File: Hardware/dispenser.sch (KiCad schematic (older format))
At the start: 60 parts, among them J1 Vin, J2 encoder+btn, J3 YuMi_interface, J4 Motor, U1 SN74LVC1G14, U2 LM2675, U3 PC817, U4 ATMEGA328P-AU-Arduino, U5 PC817, U6 A4973, U7 PC817, U8 SN74LVC1G14, U9 SN74LVC1G14, Y1 8MHZ

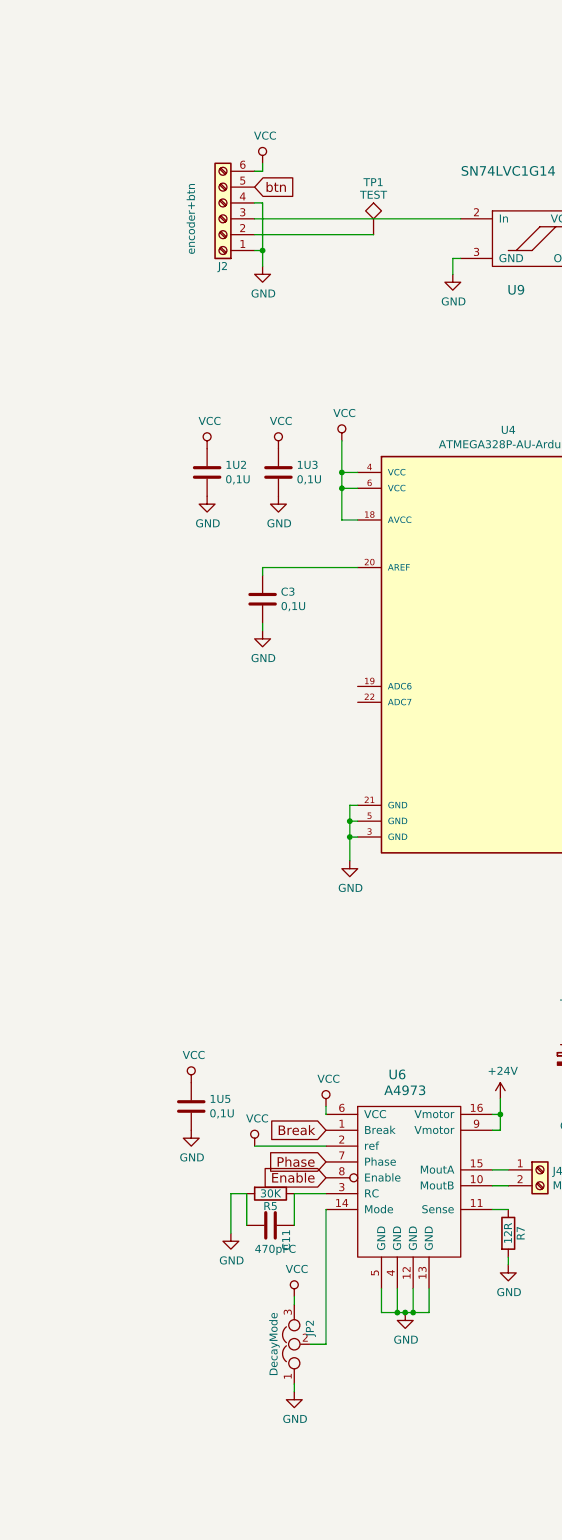
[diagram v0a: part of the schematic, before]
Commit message: added limitswitches
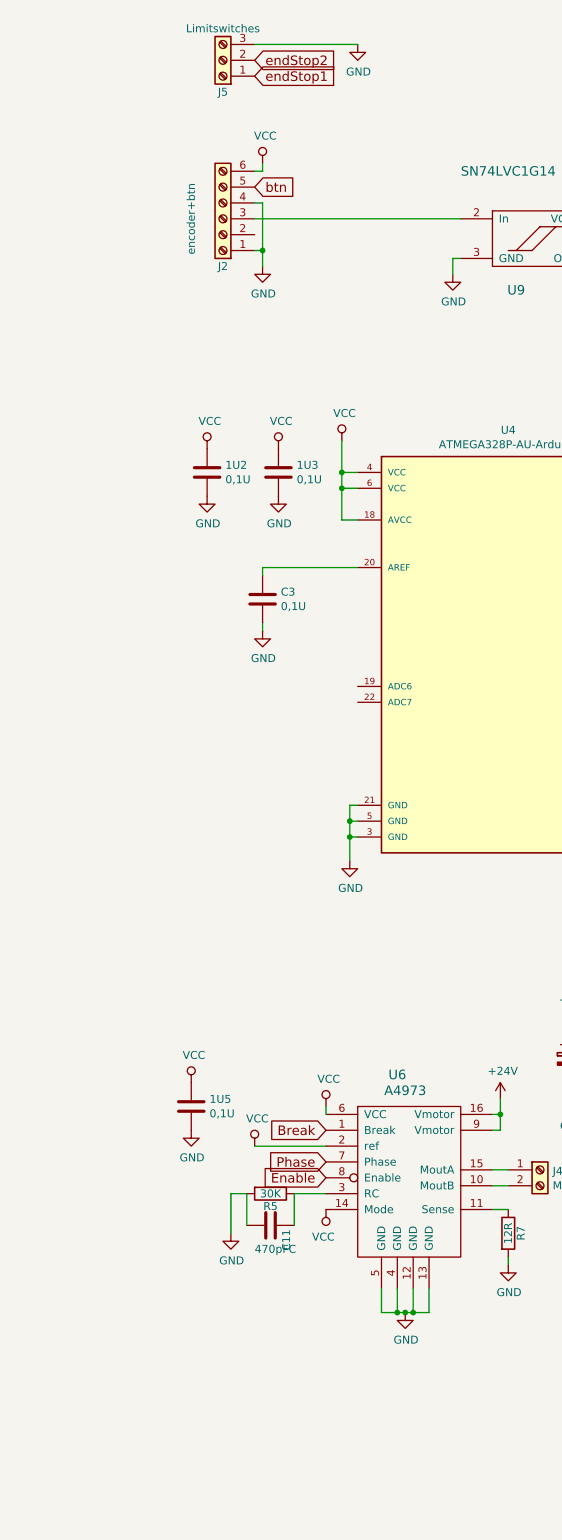
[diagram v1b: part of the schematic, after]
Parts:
- removed JP2: DecayMode, jumper:SOLDER-JUMPER_2-WAY, symbol Jumper_NC_Dual
- removed TP1: TEST, Socket_Strips:Socket_Strip_Angled_1x01_Pitch2.54mm, symbol TEST
- added J5: Limitswitches, Pin_Headers:Pin_Header_Straight_1x03_Pitch2.54mm, symbol Screw_Terminal_01x03
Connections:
- net GND: now also J5.3 (Pin_3)
- net VCC: now also U6.14 (Mode)
- new net endStop1: J5.1 (Pin_1)
- new net endStop2: J5.2 (Pin_2)
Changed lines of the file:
@@
 LIBS:L298N
 LIBS:WS2812B
+LIBS:a4973
 LIBS:dispenser-cache
 EELAYER 25 0
@@
 	11600 1800 11600 2200
 Wire Wire Line
-	11550 2000 12300 2000
-Wire Wire Line
 	1700 1250 1700 1450
 Wire Wire Line
@@
 	14050 7000 14050 7050
 $Comp
-L Jumper_NC_Dual JP2
-U 1 1 5A0A3D14
-P 11800 9000
-F 0 "JP2" H 11850 8900 50  0000 L CNN
-F 1 "DecayMode" H 11800 9100 50  0000 C BNN
-F 2 "jumper:SOLDER-JUMPER_2-WAY" H 11800 9000 50  0001 C CNN
-F 3 "" H 11800 9000 50  0001 C CNN
-	1    11800 9000
-	0    -1   -1   0
-$EndComp
-$Comp
-L GND #PWR044
-U 1 1 5A0A3E41
-P 11800 9300
-F 0 "#PWR044" H 11800 9050 50  0001 C CNN
-F 1 "GND" H 11805 9127 50  0000 C CNN
-F 2 "" H 11800 9300 50  0001 C CNN
-F 3 "" H 11800 9300 50  0001 C CNN
-	1    11800 9300
-	1    0    0    -1
-$EndComp
-Wire Wire Line
-	11800 9250 11800 9300
-$Comp
 L VCC #PWR045
 U 1 1 5A0A4017
-P 11800 8700
-F 0 "#PWR045" H 11800 8550 50  0001 C CNN
-F 1 "VCC" H 11817 8873 50  0000 C CNN
-F 2 "" H 11800 8700 50  0001 C CNN
-F 3 "" H 11800 8700 50  0001 C CNN
-	1    11800 8700
-	1    0    0    -1
-$EndComp
-Wire Wire Line
-	11800 8750 11800 8700
-Wire Wire Line
-	11900 9000 12000 9000
-Wire Wire Line
-	12000 9000 12000 8150
+P 12000 8150
+F 0 "#PWR045" H 12000 8000 50  0001 C CNN
+F 1 "VCC" H 12017 8323 50  0000 C CNN
+F 2 "" H 12000 8150 50  0001 C CNN
+F 3 "" H 12000 8150 50  0001 C CNN
+	1    12000 8150
+	-1   0    0    1
+$EndComp
 $Comp
 L R R7
@@
 	12800 2150 12800 2250
 $Comp
-L TEST TP1
-U 1 1 5A0B3992
-P 12300 2000
-F 0 "TP1" H 12300 2300 50  0000 C BNN
-F 1 "TEST" H 12300 2250 50  0000 C CNN
-F 2 "Socket_Strips:Socket_Strip_Angled_1x01_Pitch2.54mm" H 12300 2000 50  0001 C CNN
-F 3 "" H 12300 2000 50  0001 C CNN
-	1    12300 2000
-	1    0    0    -1
-$EndComp
-$Comp
 L LM2675 U2
 U 1 1 5A169D00
@@
 Wire Notes Line
 	5650 10950 3200 10950
+$Comp
+L Screw_Terminal_01x03 J5
+U 1 1 5A1FD8A3
+P 11350 900
+F 0 "J5" H 11350 1100 50  0000 C CNN
+F 1 "Limitswitches" H 11350 700 50  0000 C CNN
+F 2 "Pin_Headers:Pin_Header_Straight_1x03_Pitch2.54mm" H 11350 900 50  0001 C CNN
+F 3 "" H 11350 900 50  0001 C CNN
+	1    11350 900
+	-1   0    0    1
+$EndComp
+Text GLabel 11550 1000 2    60   Input ~ 0
+endStop1
+Text GLabel 11550 900  2    60   Input ~ 0
+endStop2
+$Comp
+L GND #PWR062
+U 1 1 5A1FDD4B
+P 12200 800
+F 0 "#PWR062" H 12200 550 50  0001 C CNN
+F 1 "GND" H 12205 627 50  0000 C CNN
+F 2 "" H 12200 800 50  0001 C CNN
+F 3 "" H 12200 800 50  0001 C CNN
+	1    12200 800
+	1    0    0    -1
+$EndComp
+Wire Wire Line
+	12200 800  11550 800
 $EndSCHEMATC

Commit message: sync old atmega files
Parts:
- removed C11: 470pFC, Capacitors_SMD:C_0805_HandSoldering, symbol C
- removed C12: 47uf, Capacitors_Tantalum_SMD:CP_Tantalum_Case-D_EIA-7343-31_Hand, symbol CP
- removed C13: 330Uf, Capacitors_SMD:CP_Elec_10x10, symbol CP
- removed C7: 4.7uF tant, Capacitors_Tantalum_SMD:CP_Tantalum_Case-C_EIA-6032-28_Hand, symbol CP
- removed C8: 10nf, Capacitors_SMD:C_0805_HandSoldering, symbol C_Small
- removed D5: D_Schottky, Diodes_SMD:D_SMC_Handsoldering, symbol D_Schottky
- removed J2: encoder+btn, Pin_Headers:Pin_Header_Straight_1x06_Pitch2.54mm, symbol Screw_Terminal_01x06
- removed J5: Limitswitches, Pin_Headers:Pin_Header_Straight_1x03_Pitch2.54mm, symbol Screw_Terminal_01x03
- removed L1: 47uH, Inductors_SMD:L_7.3x7.3_H4.5, symbol L
- removed R10: 3K, Resistors_SMD:R_0805_HandSoldering, symbol R
- removed U1, U8, U9: SN74LVC1G14, TO_SOT_Packages_SMD:SOT-23-5_HandSoldering, symbol SN74LVC1G14
- removed U2: LM2675, Housings_SOIC:SOIC-8_3.9x4.9mm_Pitch1.27mm, symbol LM2675
- removed U6: A4973, Housings_SOIC:SOIC-16W_7.5x10.3mm_Pitch1.27mm, symbol A4973
- added C7, C8: 47nF, Capacitors_SMD:C_0805_HandSoldering, symbol C
- added D6, D7, D8, D9: D, Diodes_SMD:D_SMA-SMB_Universal_Handsoldering, symbol D
- added IC1: L298N, Libs:Multiwatt15_V, symbol L298N
- added ISP1: ISP-header, Pin_Headers:Pin_Header_Straight_2x03_Pitch2.54mm, symbol ISP-header
- added J2: encoder_in, Socket_Strips:Socket_Strip_Straight_1x04_Pitch2.54mm, symbol Screw_Terminal_01x04
- added J5: OELD, Pin_Headers:Pin_Header_Straight_1x04_Pitch2.54mm, symbol Conn_01x04
- added R13, R14: 100K, Resistors_SMD:R_0805_HandSoldering, symbol R
- added R17, R18: 4k7, Resistors_SMD:R_0805_HandSoldering, symbol R
- added U1: 74HC14, Housings_DIP:DIP-14_W7.62mm_LongPads, symbol 74HC14
- added U2: AMS117-5.0, TO_SOT_Packages_SMD:SOT-223, symbol AMS117-5.0
- added U6: LM321, TO_SOT_Packages_SMD:SOT-23-5, symbol LM321
- 1U1: value 0.1uf -> 1U
- C1: value 4.7uF tant -> 22uf; footprint Capacitors_Tantalum_SMD:CP_Tantalum_Case-C_EIA-6032-28_Hand -> Capacitors_Tantalum_SMD:CP_Tantalum_Case-D_EIA-7343-31_Hand
- C5: value 47uf -> 22uf
- D2, D4: footprint LEDs:LED_0805_HandSoldering -> LEDs:LED_D3.0mm
- JP1: footprint Pin_Headers:Pin_Header_Straight_2x01_Pitch2.54mm -> jumper:SOLDER-JUMPER_1-WAY
- R5: value 30K -> 330K
- R7: value 12R -> 6k8
- R8: value 1K -> 1R; footprint Resistors_SMD:R_0805_HandSoldering -> Resistors_THT:R_Axial_DIN0516_L15.5mm_D5.0mm_P20.32mm_Horizontal
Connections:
- net +24V: now also D6.1 (K), D7.1 (K), IC1.4 (VS), U2.3 (Vin); no longer C1.1
- net CMD: now also U1.8
- net GND: now also C7.2, C8.2, D8.2 (A), D9.2 (A), IC1.10 (INPUT3), IC1.11 (ENABLE_B), IC1.12 (INPUT4), IC1.15 (SEN_B), IC1.8 (GND), ISP1.6 (GND), J2.1 (Pin_1), J5.4 (Pin_4), U1.11, U1.13, U1.7 (GND), U1.7 (GND), U1.7 (GND), U1.7 (GND), U1.7 (GND), U1.7 (GND), U2.1 (GND), U6.2 (V-); no longer D3.1 (VSS), R5.2
- net LED: no longer D3.2 (DIN)
- net MISO: now also ISP1.1 (MISO)
- net MOSI: now also ISP1.4 (MOSI)
- net SCK: now also ISP1.3 (SCK)
- net Step: now also U1.6
- net VCC: now also C1.1, IC1.9 (VCC), ISP1.2 (VCC), J2.4 (Pin_4), J5.1 (Pin_1), R13.1, R14.1, R17.1, R18.1, U1.14 (VCC), U1.14 (VCC), U1.14 (VCC), U1.14 (VCC), U1.14 (VCC), U1.14 (VCC), U2.2 (Vout), U6.5 (V+); no longer D3.3 (VDD)
- net encA: now also U1.2
- net reset_in: now also ISP1.5 (RST)
- net at U4.22 (ADC7): now also R5.1, U6.4
- net sda: now reaches U4.27 (A4/18)
- net sda: now also J5.2 (Pin_2), R18.2
- net scl: now reaches U4.28 (A5/19/SCL)
- net scl: now also J5.3 (Pin_3), R17.2
- net at J4.1 (Pin_1): now also D6.2 (A), D8.1 (K), IC1.2 (OUT1)
- net at J4.2 (Pin_2): now also D7.2 (A), D9.1 (K), IC1.3 (OUT2)
- net at C9.1, D11.1 (K), R15.2: now also U1.9
- net at C10.1, D12.1 (K), R16.2: now also U1.5
- net at R7.1: now also R5.2, U6.3 (-)
- net current: now reaches R8.2
- net current: now also IC1.1 (SEN_A), U6.1 (+)
- net Break renamed en
- net en: now also IC1.6 (ENABLE_A)
- net Enable renamed in1
- net in1: now also IC1.5 (INPUT1)
- net Phase renamed in2
- net in2: now also IC1.7 (INPUT2)
- net btn: no longer names the net of U4.12 (8)
- new net: C8.1, J2.2 (Pin_2), R14.2, U1.3
- new net: C7.1, J2.3 (Pin_3), R13.2, U1.1
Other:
- note added: "5v logic 24 mA\n\nVin:24v 0.6W heat ?"
- note added: "OLED LCD \nBehöver jag verkligen denna?\n"
- note removed: "?\n"
- note removed: "Itrip = Vref / 2xRsense\n\n208mA = 5V/12 Ohm"
- moved on the sheet: 1U5, 1U6, C5, J4
